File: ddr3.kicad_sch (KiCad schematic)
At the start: 49 parts, among them U201 xc7z010clg400, U301 MT41K256M16TW-107_P

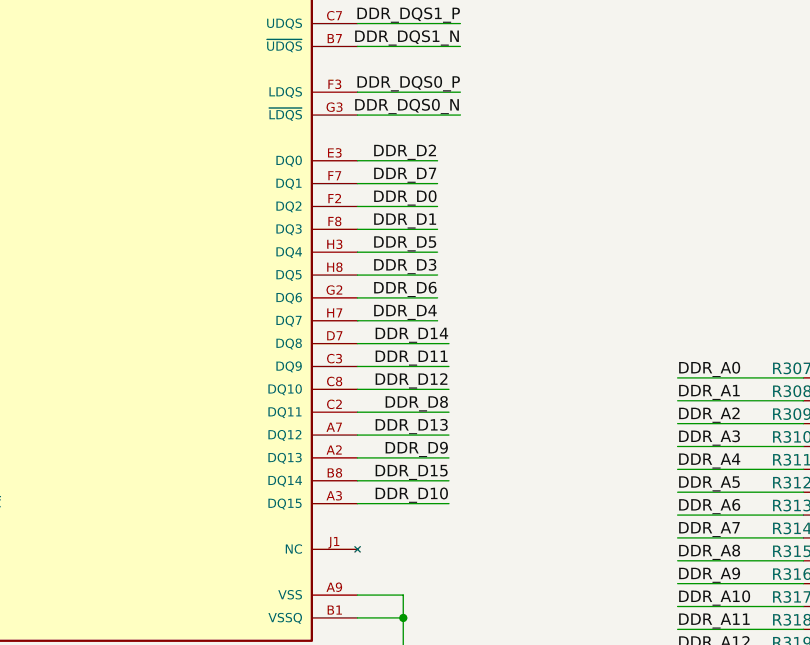
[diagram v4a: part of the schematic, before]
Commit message: feat: finish basic ddr3 routing
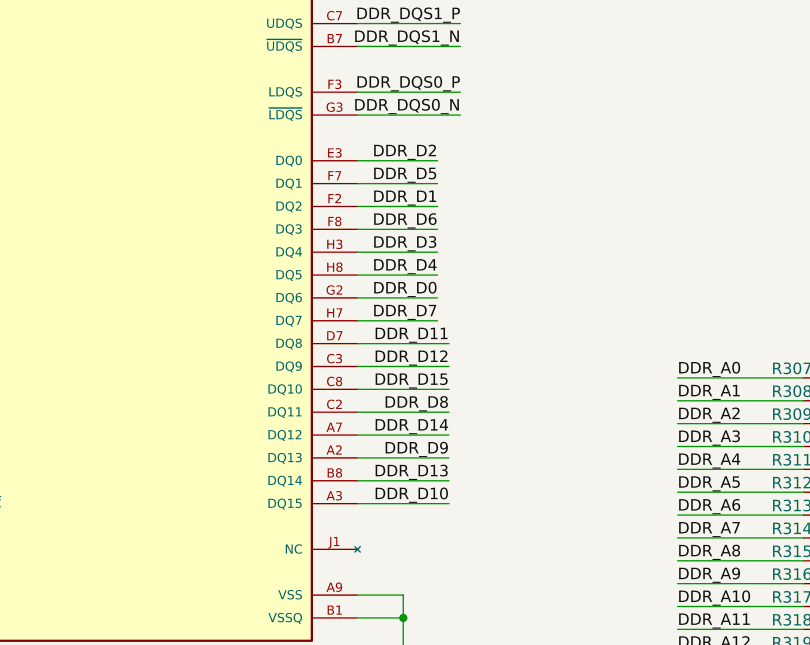
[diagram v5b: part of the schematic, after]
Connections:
- net DDR_D0: now also U301.G2 (DQ6); no longer U301.F2 (DQ2)
- net DDR_D1: now also U301.F2 (DQ2); no longer U301.F8 (DQ3)
- net DDR_D11: now also U301.D7 (DQ8); no longer U301.C3 (DQ9)
- net DDR_D12: now also U301.C3 (DQ9); no longer U301.C8 (DQ10)
- net DDR_D13: now also U301.B8 (DQ14); no longer U301.A7 (DQ12)
- net DDR_D14: now also U301.A7 (DQ12); no longer U301.D7 (DQ8)
- net DDR_D15: now also U301.C8 (DQ10); no longer U301.B8 (DQ14)
- net DDR_D3: now also U301.H3 (DQ4); no longer U301.H8 (DQ5)
- net DDR_D4: now also U301.H8 (DQ5); no longer U301.H7 (DQ7)
- net DDR_D5: now also U301.F7 (DQ1); no longer U301.H3 (DQ4)
- net DDR_D6: now also U301.F8 (DQ3); no longer U301.G2 (DQ6)
- net DDR_D7: now also U301.H7 (DQ7); no longer U301.F7 (DQ1)
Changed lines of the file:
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@@
 	)
 	(label "DDR_D1"
-		(at 116.84 139.7 180)
+		(at 116.84 137.16 180)
 		(effects
 			(font
@@
 	)
 	(label "DDR_D5"
-		(at 116.84 142.24 180)
+		(at 116.84 134.62 180)
 		(effects
 			(font
@@
 	)
 	(label "DDR_D13"
-		(at 118.11 162.56 180)
+		(at 118.11 167.64 180)
 		(effects
 			(font
@@
 	)
 	(label "DDR_D6"
-		(at 116.84 147.32 180)
+		(at 116.84 139.7 180)
 		(effects
 			(font
@@
 	)
 	(label "DDR_D14"
-		(at 118.11 152.4 180)
+		(at 118.11 162.56 180)
 		(effects
 			(font
@@
 	)
 	(label "DDR_D11"
-		(at 118.11 154.94 180)
+		(at 118.11 152.4 180)
 		(effects
 			(font
@@
 	)
 	(label "DDR_D0"
-		(at 116.84 137.16 180)
+		(at 116.84 147.32 180)
 		(effects
 			(font
@@
 	)
 	(label "DDR_D4"
-		(at 116.84 149.86 180)
+		(at 116.84 144.78 180)
 		(effects
 			(font
@@
 	)
 	(label "DDR_D15"
-		(at 118.11 167.64 180)
+		(at 118.11 157.48 180)
 		(effects
 			(font
@@
 	)
 	(label "DDR_D7"
-		(at 116.84 134.62 180)
+		(at 116.84 149.86 180)
 		(effects
 			(font
@@
 	)
 	(label "DDR_D3"
-		(at 116.84 144.78 180)
+		(at 116.84 142.24 180)
 		(effects
 			(font
@@
 	)
 	(label "DDR_D12"
-		(at 118.11 157.48 180)
+		(at 118.11 154.94 180)
 		(effects
 			(font
@@
 	)
 	(group ""
+		(members "0187cd6e-3035-46bc-a543-d863123f6aa6" "1205eb99-5061-4fde-9d52-430c0e9eaf27"
+			"1428bb5b-25ee-4e1c-af90-0ec7ab619755" "181118db-3141-4fd0-ab41-95b82ea9a367"
+			"2bf5c511-b95c-4bee-a7c6-316f429118e3" "36f116a2-68bc-498b-b9c5-bacb81fe160f"
+			"5019861b-f472-4d54-a558-11a102c6ef85" "5c7550ea-6813-4580-9059-4666512b1019"
+			"6079ba45-e1ad-4d2e-8a67-72c96c3e62a6" "61b16fff-c865-45b7-8a6e-c7c27907bdb9"
+			"67c70d83-02f9-4af6-9a55-7edf6e9f5254" "77c5435b-3cbc-46b4-8801-451abcf91890"
+			"83b3a111-9159-4e38-936c-7b2e67099b73" "8d9902ab-d7da-4dec-92bf-ad7503c3a608"
+			"92bda92a-c974-49b0-a4a1-5138d8f63e38" "aefed6be-4028-4577-8d6e-bc7993c29b33"
+			"afc52c06-7b61-4487-bd3d-0437d6197051" "b09c7023-4bf6-49af-a4d0-0f29e4ed17dc"
+			"ba34789e-cf04-442a-b8f2-44e84dde138b" "c551c309-af21-4f81-a772-98b47ac10157"
+			"cd7cb585-1640-4391-998a-8578013a16a3" "d3b38538-3fba-4c4a-a8b7-878a51d25623"
+			"d5a9b04a-69a2-4b62-8b02-cb554a74a1e9" "da064704-32c3-412d-be85-da6c9e2cb2dc"
+			"e35295c4-f9ed-4f63-a6b8-da27db2fd70b" "e7a3f6c5-1c81-4f2c-af93-168af3e34968"
+			"f05a3304-9bab-4088-804f-df5b2f008ce1" "f1402273-dc22-43c7-ba42-ea3280383b97"
+			"fb7af934-3c08-46d8-bc48-0d34a4eb09c0"
+		)
+	)
+	(group ""
+		(members "7ccb2fe3-cb20-4333-b8b9-98d84b63af3b" "d37502c3-5590-493a-bc38-3d4a5c966a94"
+			"faf0e304-8304-4196-a462-0dc4c833cb45"
+		)
+	)
+	(group ""
 		(members "0afbe7b4-aff3-434a-9df5-3e315ce423e6" "118f631a-09d0-4557-9133-2f6a93c0060b"
 			"133bed2b-7b91-4793-85df-a1ce4ec4429c" "1e2ad878-b695-425b-8b5c-cd812e06d1c2"
@@
 		)
 	)
+	(group ""
+		(members "1aaf9853-f857-47f0-a547-4514794eb91f" "80056e34-546a-424f-878a-a528d511a14b"
+			"98920988-14a5-442a-8623-6c6a1590815c" "cd9805dd-722e-4722-9e08-159a2864cb19"
+		)
+	)
+	(group ""
+		(members "336734b5-4ef0-4ce9-a935-45fa11f72620" "e966fc0b-3074-43d0-afe5-d1d580d28e80")
+	)
+	(group ""
+		(members "2cb76e46-4327-436f-83b1-71eb2389e897" "378a093b-0387-4256-8bca-5dcaa8c30a38"
+			"50b3db6d-07e4-4dac-8942-c12e390492b9" "610c0ce5-8b88-4d30-a8c1-788c9d0811f0"
+			"6afc9b1c-08a7-40d7-ac83-5ca7a6a29088" "6bd9b869-c348-4ca8-a17e-6435df665d8d"
+			"74180daa-144a-44d4-af84-4a51a246cee4" "7731ab3f-97b9-444a-bbff-0965e4909245"
+			"a0e7dfbc-7101-4ee1-8880-d61b616816eb" "a534bcf1-4fdf-4204-b1da-bf890d83c5fc"
+			"af65d9cc-204c-4ea0-aabe-4c5a343c9bf2" "ceb93b8e-4eed-4e41-8d36-b6b9b9426cdc"
+			"defbf65e-8b75-475e-b0d6-f20581a43479" "efc63aa4-c45f-474f-b31e-49b5211dbd9e"
+			"f9490e51-9506-42f8-9149-953780794549"
+		)
+	)
+	(group ""
+		(members "19bab4db-9792-4038-9742-4d4a062007fb" "21305b34-e691-4b51-bea9-04e45c0ea4b8"
+			"4849c74f-895a-4e72-94ab-b2c034e74c74" "574b87e8-ebda-4b42-b5d5-ec59f9533378"
+			"590b2a1d-9fb8-4d04-93af-41a0b14869b6" "62051dbd-0e98-48e1-b812-0a06478769ee"
+			"75a2595a-ea45-4c86-9c82-30c1ace53176" "869b8400-d186-480d-9a6e-00a8aed98c20"
+			"a37322bd-9ea8-474d-b674-a4d477214c96" "b4cbc500-5438-442e-b577-3bb986520e4e"
+			"be489095-e1a8-4d83-9bcc-e8e35321c198" "cc6d000a-e1a3-433d-b8bc-99704b09c34d"
+			"d0285f44-4ce2-4b2b-9619-c97a22fe7ebb" "d48d75fd-fb5b-4864-b9c0-308323867e60"
+			"d7dce211-4904-4327-bc57-437848297cf4" "d873919b-ae19-44d8-9c4b-dee99b23b790"
+		)
+	)
